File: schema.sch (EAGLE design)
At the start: 9 parts

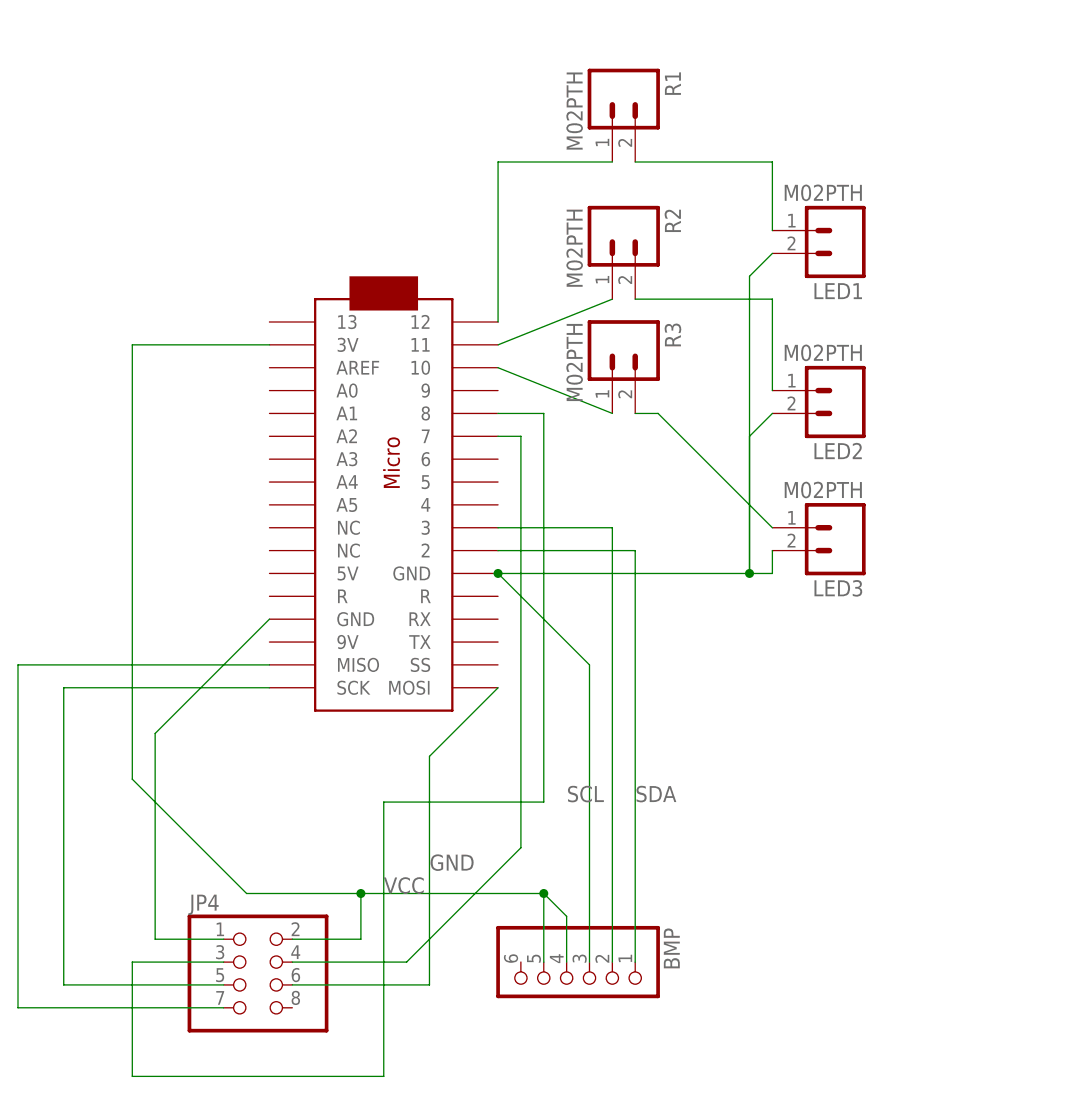
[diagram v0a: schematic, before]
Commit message: ERNEST v0.2
Added a DIP switch for quick setting of the node ID, to avoid
having to reflash the thing each time.
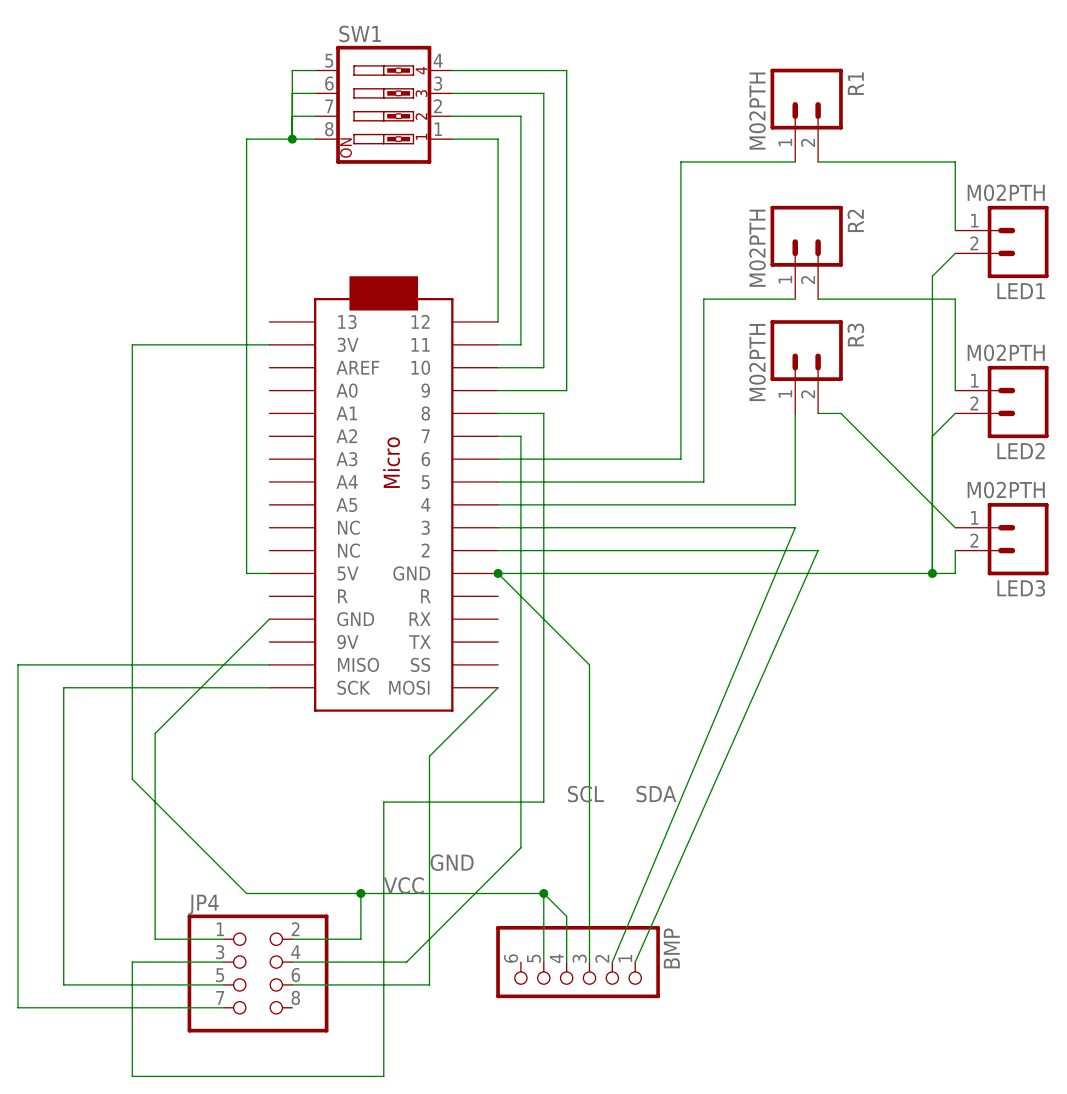
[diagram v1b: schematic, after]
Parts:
- added SW1: (no value), special:SW_DIP-4
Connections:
- new net N$1: R3.1, U$1.4
- new net N$14: SW1.2, U$1.11
- new net N$15: SW1.3, U$1.10
- new net N$16: SW1.4, U$1.9
- new net N$8: R2.1, U$1.5
- net N$11: now also U$1.6; no longer R3.1, U$1.10
- net N$12: now also SW1.5, SW1.6, SW1.7, SW1.8, U$1.5V; no longer R2.1, U$1.11
- net N$13: now also SW1.1; no longer R1.1
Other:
- moved on the sheet: LED1, LED2, LED3, R1, R2, R3
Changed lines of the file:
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@@
 <part name="R2" library="SparkFun-Connectors" deviceset="M02" device="PTH"/>
 <part name="R3" library="SparkFun-Connectors" deviceset="M02" device="PTH"/>
+<part name="SW1" library="special" deviceset="SW_DIP-4" device=""/>
 </parts>
 <sheets>
@@
 <attribute name="VALUE" x="48.26" y="8.89" size="1.778" layer="96" rot="R270"/>
 </instance>
-<instance part="LED1" gate="G$1" x="88.9" y="86.36" rot="R180"/>
-<instance part="LED2" gate="G$1" x="88.9" y="68.58" rot="R180"/>
-<instance part="LED3" gate="G$1" x="88.9" y="53.34" rot="R180"/>
-<instance part="R1" gate="G$1" x="63.5" y="101.6" rot="R270"/>
-<instance part="R2" gate="G$1" x="63.5" y="86.36" rot="R270"/>
-<instance part="R3" gate="G$1" x="63.5" y="73.66" rot="R270"/>
+<instance part="LED1" gate="G$1" x="109.22" y="86.36" rot="R180"/>
+<instance part="LED2" gate="G$1" x="109.22" y="68.58" rot="R180"/>
+<instance part="LED3" gate="G$1" x="109.22" y="53.34" rot="R180"/>
+<instance part="R1" gate="G$1" x="83.82" y="101.6" rot="R270"/>
+<instance part="R2" gate="G$1" x="83.82" y="86.36" rot="R270"/>
+<instance part="R3" gate="G$1" x="83.82" y="73.66" rot="R270"/>
+<instance part="SW1" gate="A" x="38.1" y="101.6"/>
 </instances>
 <busses>
@@
 <segment>
 <pinref part="BMP" gate="A" pin="2"/>
-<wire x1="63.5" y1="5.08" x2="63.5" y2="53.34" width="0.1524" layer="91"/>
+<wire x1="63.5" y1="5.08" x2="83.82" y2="53.34" width="0.1524" layer="91"/>
 <label x="58.42" y="22.86" size="1.778" layer="95"/>
 <pinref part="U$1" gate="G$1" pin="3"/>
-<wire x1="50.8" y1="53.34" x2="63.5" y2="53.34" width="0.1524" layer="91"/>
+<wire x1="50.8" y1="53.34" x2="83.82" y2="53.34" width="0.1524" layer="91"/>
 </segment>
 </net>
@@
 <segment>
 <pinref part="BMP" gate="A" pin="1"/>
-<wire x1="66.04" y1="50.8" x2="66.04" y2="5.08" width="0.1524" layer="91"/>
+<wire x1="86.36" y1="50.8" x2="66.04" y2="5.08" width="0.1524" layer="91"/>
 <label x="66.04" y="22.86" size="1.778" layer="95"/>
 <pinref part="U$1" gate="G$1" pin="2"/>
-<wire x1="66.04" y1="50.8" x2="50.8" y2="50.8" width="0.1524" layer="91"/>
+<wire x1="86.36" y1="50.8" x2="50.8" y2="50.8" width="0.1524" layer="91"/>
 </segment>
 </net>
@@
 <pinref part="R1" gate="G$1" pin="2"/>
 <pinref part="LED1" gate="G$1" pin="1"/>
-<wire x1="66.04" y1="93.98" x2="81.28" y2="93.98" width="0.1524" layer="91"/>
-<wire x1="81.28" y1="93.98" x2="81.28" y2="86.36" width="0.1524" layer="91"/>
+<wire x1="86.36" y1="93.98" x2="101.6" y2="93.98" width="0.1524" layer="91"/>
+<wire x1="101.6" y1="93.98" x2="101.6" y2="86.36" width="0.1524" layer="91"/>
 </segment>
 </net>
@@
 <pinref part="R2" gate="G$1" pin="2"/>
 <pinref part="LED2" gate="G$1" pin="1"/>
-<wire x1="66.04" y1="78.74" x2="81.28" y2="78.74" width="0.1524" layer="91"/>
-<wire x1="81.28" y1="78.74" x2="81.28" y2="68.58" width="0.1524" layer="91"/>
+<wire x1="86.36" y1="78.74" x2="101.6" y2="78.74" width="0.1524" layer="91"/>
+<wire x1="101.6" y1="78.74" x2="101.6" y2="68.58" width="0.1524" layer="91"/>
 </segment>
 </net>
@@
 <pinref part="R3" gate="G$1" pin="2"/>
 <pinref part="LED3" gate="G$1" pin="1"/>
-<wire x1="66.04" y1="66.04" x2="68.58" y2="66.04" width="0.1524" layer="91"/>
-<wire x1="68.58" y1="66.04" x2="81.28" y2="53.34" width="0.1524" layer="91"/>
+<wire x1="86.36" y1="66.04" x2="88.9" y2="66.04" width="0.1524" layer="91"/>
+<wire x1="88.9" y1="66.04" x2="101.6" y2="53.34" width="0.1524" layer="91"/>
 </segment>
 </net>
@@
 <wire x1="60.96" y1="5.08" x2="60.96" y2="38.1" width="0.1524" layer="91"/>
 <wire x1="60.96" y1="38.1" x2="50.8" y2="48.26" width="0.1524" layer="91"/>
-<wire x1="50.8" y1="48.26" x2="78.74" y2="48.26" width="0.1524" layer="91"/>
+<wire x1="50.8" y1="48.26" x2="99.06" y2="48.26" width="0.1524" layer="91"/>
 <junction x="50.8" y="48.26"/>
 <pinref part="LED3" gate="G$1" pin="2"/>
-<wire x1="78.74" y1="48.26" x2="81.28" y2="48.26" width="0.1524" layer="91"/>
-<wire x1="81.28" y1="48.26" x2="81.28" y2="50.8" width="0.1524" layer="91"/>
+<wire x1="99.06" y1="48.26" x2="101.6" y2="48.26" width="0.1524" layer="91"/>
+<wire x1="101.6" y1="48.26" x2="101.6" y2="50.8" width="0.1524" layer="91"/>
 <pinref part="LED2" gate="G$1" pin="2"/>
-<wire x1="78.74" y1="48.26" x2="78.74" y2="63.5" width="0.1524" layer="91"/>
-<wire x1="78.74" y1="63.5" x2="81.28" y2="66.04" width="0.1524" layer="91"/>
-<junction x="78.74" y="48.26"/>
+<wire x1="99.06" y1="48.26" x2="99.06" y2="63.5" width="0.1524" layer="91"/>
+<wire x1="99.06" y1="63.5" x2="101.6" y2="66.04" width="0.1524" layer="91"/>
+<junction x="99.06" y="48.26"/>
 <pinref part="LED1" gate="G$1" pin="2"/>
-<wire x1="78.74" y1="48.26" x2="78.74" y2="81.28" width="0.1524" layer="91"/>
-<wire x1="78.74" y1="81.28" x2="81.28" y2="83.82" width="0.1524" layer="91"/>
+<wire x1="99.06" y1="48.26" x2="99.06" y2="81.28" width="0.1524" layer="91"/>
+<wire x1="99.06" y1="81.28" x2="101.6" y2="83.82" width="0.1524" layer="91"/>
 </segment>
 </net>
@@
 </segment>
 </net>
+<net name="N$1" class="0">
+<segment>
+<pinref part="U$1" gate="G$1" pin="4"/>
+<pinref part="R3" gate="G$1" pin="1"/>
+<wire x1="50.8" y1="55.88" x2="83.82" y2="55.88" width="0.1524" layer="91"/>
+<wire x1="83.82" y1="55.88" x2="83.82" y2="66.04" width="0.1524" layer="91"/>
+</segment>
+</net>
+<net name="N$8" class="0">
+<segment>
+<pinref part="U$1" gate="G$1" pin="5"/>
+<wire x1="50.8" y1="58.42" x2="73.66" y2="58.42" width="0.1524" layer="91"/>
+<wire x1="73.66" y1="58.42" x2="73.66" y2="78.74" width="0.1524" layer="91"/>
+<pinref part="R2" gate="G$1" pin="1"/>
+<wire x1="73.66" y1="78.74" x2="83.82" y2="78.74" width="0.1524" layer="91"/>
+</segment>
+</net>
 <net name="N$11" class="0">
 <segment>
+<pinref part="U$1" gate="G$1" pin="6"/>
+<wire x1="50.8" y1="60.96" x2="71.12" y2="60.96" width="0.1524" layer="91"/>
+<wire x1="71.12" y1="60.96" x2="71.12" y2="93.98" width="0.1524" layer="91"/>
+<wire x1="71.12" y1="93.98" x2="83.82" y2="93.98" width="0.1524" layer="91"/>
+</segment>
+</net>
+<net name="N$12" class="0">
+<segment>
+<pinref part="U$1" gate="G$1" pin="5V"/>
+<wire x1="25.4" y1="48.26" x2="22.86" y2="48.26" width="0.1524" layer="91"/>
+<wire x1="22.86" y1="48.26" x2="22.86" y2="96.52" width="0.1524" layer="91"/>
+<wire x1="22.86" y1="96.52" x2="27.94" y2="96.52" width="0.1524" layer="91"/>
+<wire x1="27.94" y1="96.52" x2="30.48" y2="96.52" width="0.1524" layer="91"/>
+<wire x1="27.94" y1="96.52" x2="27.94" y2="99.06" width="0.1524" layer="91"/>
+<wire x1="27.94" y1="99.06" x2="30.48" y2="99.06" width="0.1524" layer="91"/>
+<junction x="27.94" y="96.52"/>
+<wire x1="27.94" y1="96.52" x2="27.94" y2="101.6" width="0.1524" layer="91"/>
+<wire x1="27.94" y1="101.6" x2="30.48" y2="101.6" width="0.1524" layer="91"/>
+<wire x1="27.94" y1="96.52" x2="27.94" y2="104.14" width="0.1524" layer="91"/>
+<wire x1="27.94" y1="104.14" x2="30.48" y2="104.14" width="0.1524" layer="91"/>
+<pinref part="SW1" gate="A" pin="5"/>
+<pinref part="SW1" gate="A" pin="6"/>
+<pinref part="SW1" gate="A" pin="7"/>
+<pinref part="SW1" gate="A" pin="8"/>
+</segment>
+</net>
+<net name="N$13" class="0">
+<segment>
+<pinref part="U$1" gate="G$1" pin="12"/>
+<wire x1="45.72" y1="96.52" x2="50.8" y2="96.52" width="0.1524" layer="91"/>
+<wire x1="50.8" y1="96.52" x2="50.8" y2="76.2" width="0.1524" layer="91"/>
+<pinref part="SW1" gate="A" pin="1"/>
+</segment>
+</net>
+<net name="N$14" class="0">
+<segment>
+<wire x1="45.72" y1="99.06" x2="53.34" y2="99.06" width="0.1524" layer="91"/>
+<wire x1="53.34" y1="99.06" x2="53.34" y2="73.66" width="0.1524" layer="91"/>
+<pinref part="U$1" gate="G$1" pin="11"/>
+<wire x1="53.34" y1="73.66" x2="50.8" y2="73.66" width="0.1524" layer="91"/>
+<pinref part="SW1" gate="A" pin="2"/>
+</segment>
+</net>
+<net name="N$15" class="0">
+<segment>
+<wire x1="45.72" y1="101.6" x2="55.88" y2="101.6" width="0.1524" layer="91"/>
+<wire x1="55.88" y1="101.6" x2="55.88" y2="71.12" width="0.1524" layer="91"/>
 <pinref part="U$1" gate="G$1" pin="10"/>
-<pinref part="R3" gate="G$1" pin="1"/>
-<wire x1="50.8" y1="71.12" x2="63.5" y2="66.04" width="0.1524" layer="91"/>
-</segment>
-</net>
-<net name="N$12" class="0">
-<segment>
-<pinref part="U$1" gate="G$1" pin="11"/>
-<pinref part="R2" gate="G$1" pin="1"/>
-<wire x1="50.8" y1="73.66" x2="63.5" y2="78.74" width="0.1524" layer="91"/>
-</segment>
-</net>
-<net name="N$13" class="0">
-<segment>
-<pinref part="U$1" gate="G$1" pin="12"/>
-<pinref part="R1" gate="G$1" pin="1"/>
-<wire x1="50.8" y1="76.2" x2="50.8" y2="93.98" width="0.1524" layer="91"/>
-<wire x1="50.8" y1="93.98" x2="63.5" y2="93.98" width="0.1524" layer="91"/>
-</segment>
-</net>
+<wire x1="55.88" y1="71.12" x2="50.8" y2="71.12" width="0.1524" layer="91"/>
+<pinref part="SW1" gate="A" pin="3"/>
+</segment>
+</net>
+<net name="N$16" class="0">
+<segment>
+<wire x1="45.72" y1="104.14" x2="58.42" y2="104.14" width="0.1524" layer="91"/>
+<wire x1="58.42" y1="104.14" x2="58.42" y2="68.58" width="0.1524" layer="91"/>
+<pinref part="U$1" gate="G$1" pin="9"/>
+<wire x1="58.42" y1="68.58" x2="50.8" y2="68.58" width="0.1524" layer="91"/>
+<pinref part="SW1" gate="A" pin="4"/>
+</segment>
+</net>
